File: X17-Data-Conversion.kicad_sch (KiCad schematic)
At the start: 18 parts, among them J1 Conn_01x05, SW1 1825910-6, U1 ABLS-8.000MHZ-B2-T, U2 STM32F091CCTx

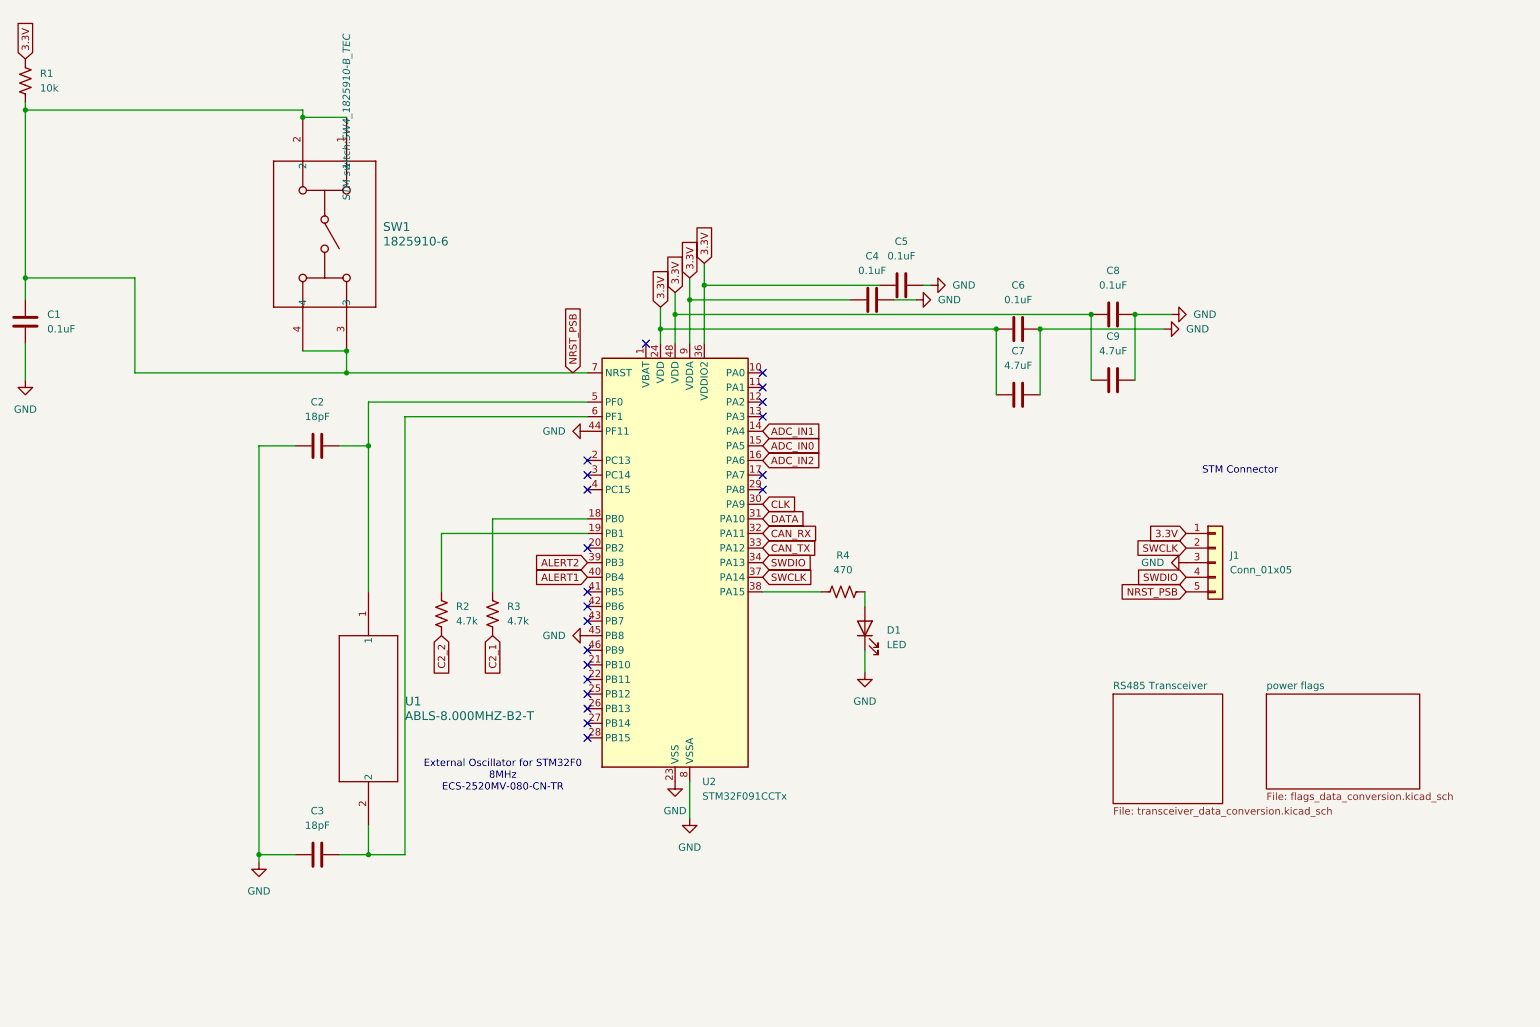
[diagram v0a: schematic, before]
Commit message: Leo's Winter break first fixes
Updates fixing the capacitor for the switch
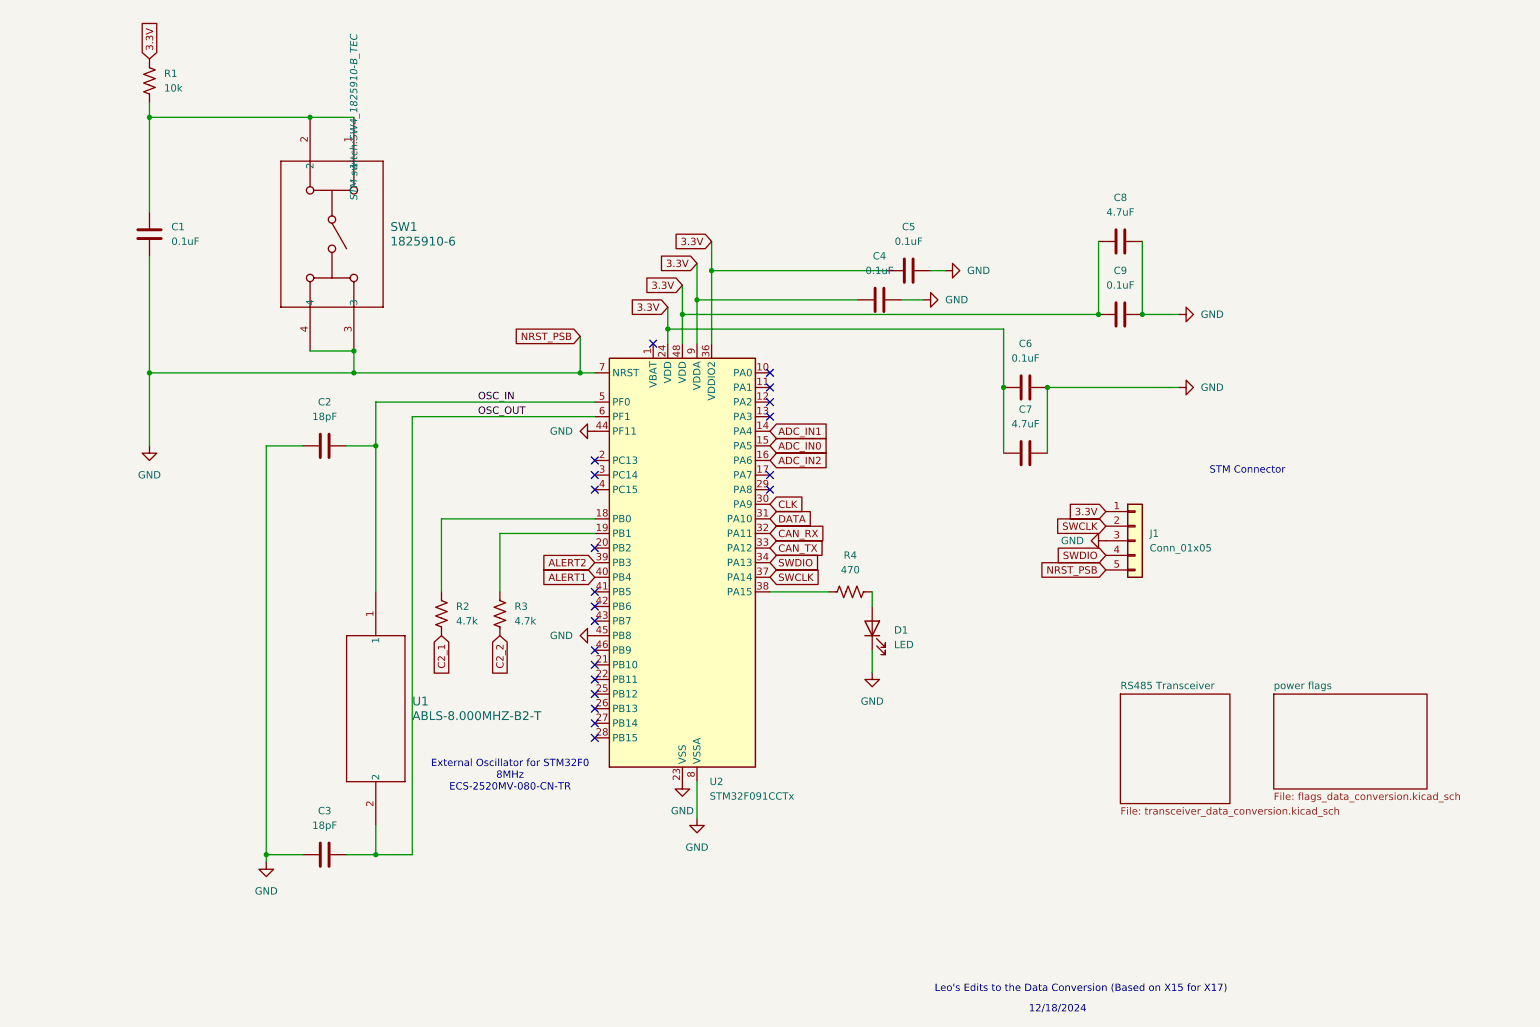
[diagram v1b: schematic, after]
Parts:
- C8: value 0.1uF -> 4.7uF
- C9: value 4.7uF -> 0.1uF
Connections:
- net C2_1: now also R2.2; no longer R3.2
- net C2_2: now also R3.2; no longer R2.2
- net GND: now also J1.5 (Pin_5), SW1.3, SW1.4, U2.7 (NRST)
- net OSC_IN: now reaches C2.1, U1.1, U2.5 (PF0)
- net OSC_OUT: now reaches C3.1, U1.2, U2.6 (PF1)
- net at U2.18 (PB0): now also R2.1; no longer R3.1
- net at U2.19 (PB1): now also R3.1; no longer R2.1
- net NRST_PSB: no longer names the net of C1.1, R1.2, SW1.1, SW1.2
- net NRST_PSB: no longer J1.5 (Pin_5), SW1.3, SW1.4, U2.7 (NRST)
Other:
- note added: "12/18/2024"
- note added: "Leo's Edits to the Data Conversion (Based on X15 for X17)"
